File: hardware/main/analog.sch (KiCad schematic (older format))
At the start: 29 parts, among them U2 LM324, U301 LM324

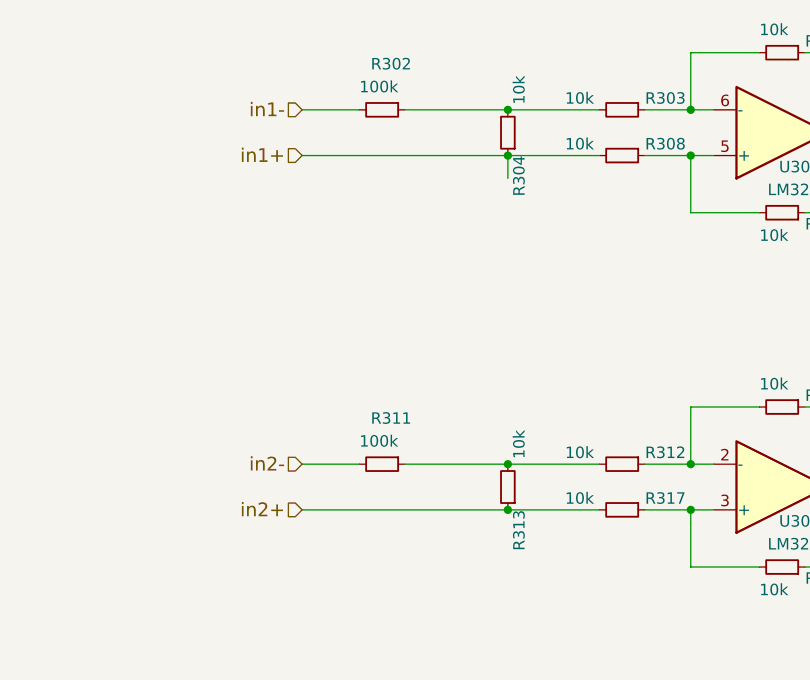
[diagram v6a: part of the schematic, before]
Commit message: Ampop gain error
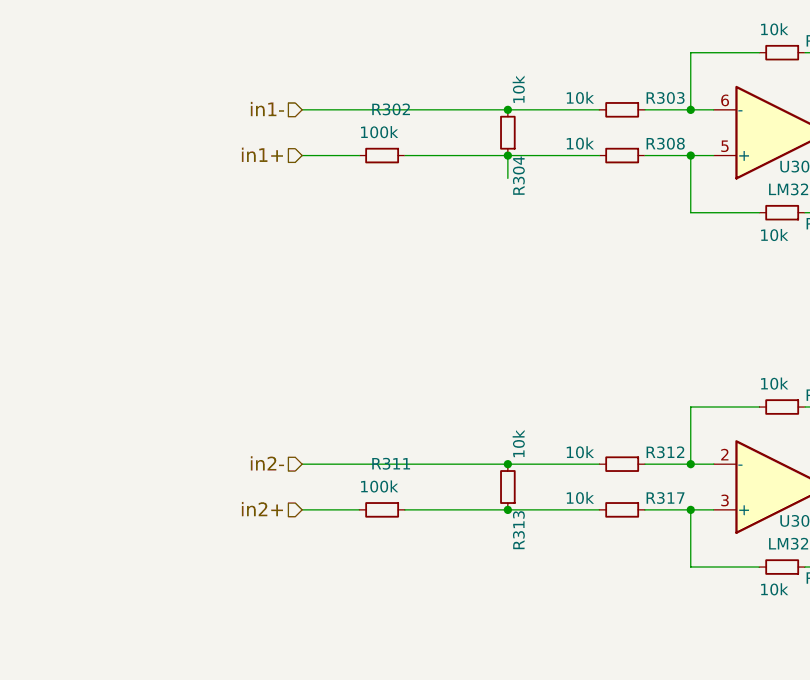
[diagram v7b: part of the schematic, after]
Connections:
- net in1+: now also R302.2; no longer R16.1, R308.2
- net in1-: now also R16.2, R303.2; no longer R302.2
- net in2+: now also R15.2; no longer R17.1, R21.2
- net in2-: now also R17.2, R20.2; no longer R15.2
- new net: R16.1, R302.1, R308.2
- new net: R15.1, R17.1, R21.2
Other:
- moved on the sheet: R302, R311
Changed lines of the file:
@@
 EESchema Schematic File Version 4
 LIBS:main-cache
-EELAYER 26 0
+EELAYER 29 0
 EELAYER END
 $Descr A4 11693 8268
@@
 $EndComp
 Wire Wire Line
-	2850 3550 3100 3550
-Wire Wire Line
-	2850 3750 3750 3750
+	2850 3750 3100 3750
 Wire Wire Line
 	4350 3550 4550 3550
@@
 Wire Wire Line
 	6750 3250 7450 3250
-Wire Wire Line
-	3300 3550 3750 3550
 $Comp
 L Amplifier_Operational:LM324 U301
@@
 L Device:R_Small R302
 U 1 1 5BE77B14
-P 3200 3550
+P 3200 3750
 AR Path="/5BE77B14" Ref="R302"  Part="1"
 AR Path="/5AAC947C/5BE77B14" Ref="R302"  Part="1"
@@
 AR Path="/5C9C4D6B/5CBAEDA0/5BE77B14" Ref="R302"  Part="1"
 AR Path="/5CBD2CE3/5CBAEDA0/5BE77B14" Ref="R?"  Part="1"
-F 0 "R302" V 3000 3500 50  0000 L CNN
-F 1 "100k" V 3100 3450 50  0000 L CNN
-F 2 "Resistor_SMD:R_0805_2012Metric_Pad1.15x1.40mm_HandSolder" H 3200 3550 50  0001 C CNN
-F 3 "" H 3200 3550 50  0001 C CNN
-	1    3200 3550
+F 0 "R302" V 3000 3700 50  0000 L CNN
+F 1 "100k" V 3100 3650 50  0000 L CNN
+F 2 "Resistor_SMD:R_0805_2012Metric_Pad1.15x1.40mm_HandSolder" H 3200 3750 50  0001 C CNN
+F 3 "" H 3200 3750 50  0001 C CNN
+	1    3200 3750
 	0    1    1    0
 $EndComp
@@
 $EndComp
 Wire Wire Line
-	2850 5100 3100 5100
-Wire Wire Line
-	2850 5300 3750 5300
+	2850 5300 3100 5300
 Wire Wire Line
 	4350 5100 4550 5100
@@
 Wire Wire Line
 	6750 4800 7450 4800
-Wire Wire Line
-	3300 5100 3750 5100
 $Comp
 L Amplifier_Operational:LM324 U?
@@
 L Device:R_Small R?
 U 1 1 5CA047C1
-P 3200 5100
+P 3200 5300
 AR Path="/5CA047C1" Ref="R?"  Part="1"
 AR Path="/5AAC947C/5CA047C1" Ref="R?"  Part="1"
@@
 AR Path="/5C9C4D6B/5CBAEDA0/5CA047C1" Ref="R311"  Part="1"
 AR Path="/5CBD2CE3/5CBAEDA0/5CA047C1" Ref="R?"  Part="1"
-F 0 "R311" V 3000 5050 50  0000 L CNN
-F 1 "100k" V 3100 5000 50  0000 L CNN
-F 2 "Resistor_SMD:R_0805_2012Metric_Pad1.15x1.40mm_HandSolder" H 3200 5100 50  0001 C CNN
-F 3 "" H 3200 5100 50  0001 C CNN
-	1    3200 5100
+F 0 "R311" V 3000 5250 50  0000 L CNN
+F 1 "100k" V 3100 5200 50  0000 L CNN
+F 2 "Resistor_SMD:R_0805_2012Metric_Pad1.15x1.40mm_HandSolder" H 3200 5300 50  0001 C CNN
+F 3 "" H 3200 5300 50  0001 C CNN
+	1    3200 5300
 	0    1    1    0
 $EndComp
@@
 	1    0    0    -1
 $EndComp
+Wire Wire Line
+	3300 3750 3750 3750
+Wire Wire Line
+	2850 3550 3750 3550
+Wire Wire Line
+	3300 5300 3750 5300
+Wire Wire Line
+	2850 5100 3750 5100
 $EndSCHEMATC
